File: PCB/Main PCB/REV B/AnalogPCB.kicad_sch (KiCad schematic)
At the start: 60 parts, among them J1 DF12NB_4.0_-20DP-0.5V_51_, J2 393570002, J3 393570002, J4 393570002, J5 393570002, J6 SJ3-35053D, Q1 2N7002, Q2 2N7002, Q3 2N7002, U1 ALDP105W, U2 ALDP105W, U3 ALDP105W

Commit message: Digital board revisions, changed to 0805 and started review of circuitry
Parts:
- removed C4: 10uF 16V X5R 0805, Capacitor_SMD:C_0805_2012Metric, symbol Device:C
- removed C?: 0.1uF 50V X7R 0805, Capacitor_SMD:C_0805_2012Metric, symbol Device:C
- removed PS2: IRM-05-5, Converter_ACDC:Converter_ACDC_MeanWell_IRM-05-xx_THT, symbol Converter_ACDC:IRM-05-5
- removed TP3: TP, TestPoint:TestPoint_Pad_D1.0mm, symbol Connector:TestPoint
- added C? (x3): 10uF 16V X5R 0805, Capacitor_SMD:C_0805_2012Metric, symbol Device:C
- added C?: 56uF 50V TH, Capacitor_THT:C_Radial_D10.0mm_H12.5mm_P5.00mm, symbol Device:C
- added L?: 5.6uH 2.9A, Customs Smoker:IND_IFSC-2020DE-01_VIS, symbol pspice:INDUCTOR
- added PS2: TSR-2-2433, Converter_DCDC:Converter_DCDC_TRACO_TSR-1_THT, symbol Regulator_Switching:TSR_1-2433
- added TP?: TP, TestPoint:TestPoint_Pad_D1.0mm, symbol Connector:TestPoint
- PS1: value IRM-10-3.3 -> IRM-10-5; Manufacturer Part Number IRM-10-3.3 -> IRM-10-5; Vendor Part Number 1866-3031-ND -> 1866-3032-ND
- gave numbers to parts that had none: 11
- renumbered D3 to D5, J2 to J1, J1 to J2, R4 to R7, R5 to R8, TP16 to TP1, TP20 to TP10, TP29 to TP11, TP18 to TP3, TP1 to TP4, TP17 to TP6, TP13 to TP7, TP15 to TP8, TP19 to TP9
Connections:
- net +3.3VA: now also C?.1, C?.2, L?.2, TP?.1; no longer C1.2, C2.1, PS1.4 (+Vo), TP4.1
- net +5V: now also C1.2, C2.1, PS1.4 (+Vo), TP4.1, PS2.1 (Vin)
- net GND: now also C?.1, C?.1, C?.2, C?.2, PS2.2 (GND)
- new net: C?.1, C?.2, L?.1, PS2.3 (Vout)
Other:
- note added: "ASSUME MEAT PROBE TIP 1-2 connection Measure resistance and room temp (1000ohms)"
- note added: "Power Delivery"
- note removed: "AC-DC MAIN"
- note removed: "ASSUME MEAT PROBE TIP 1-2 connection"
- note removed: "TODO Test this and fix"
- moved on the sheet: C1, C2, D5, D6, J1, PS1, R7, R8, TP1, TP3, TP4, TP7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

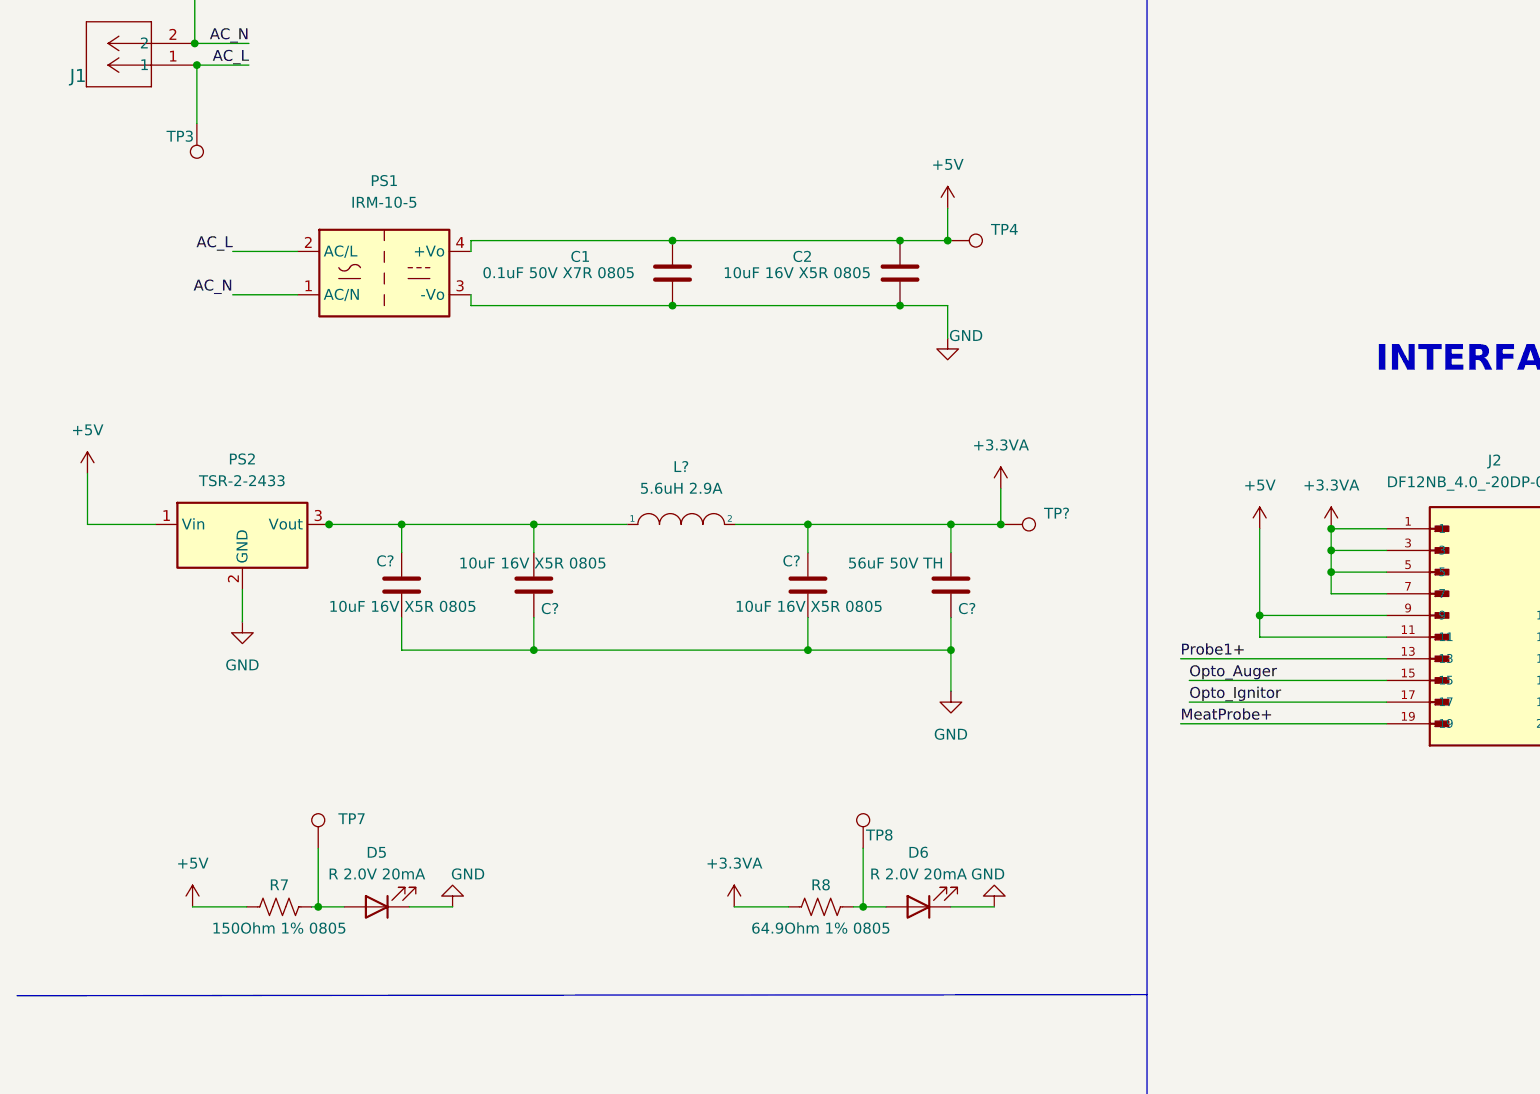
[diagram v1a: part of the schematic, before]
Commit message: begin change of power arch so mux occurs at 5.0v rather than 3.3v
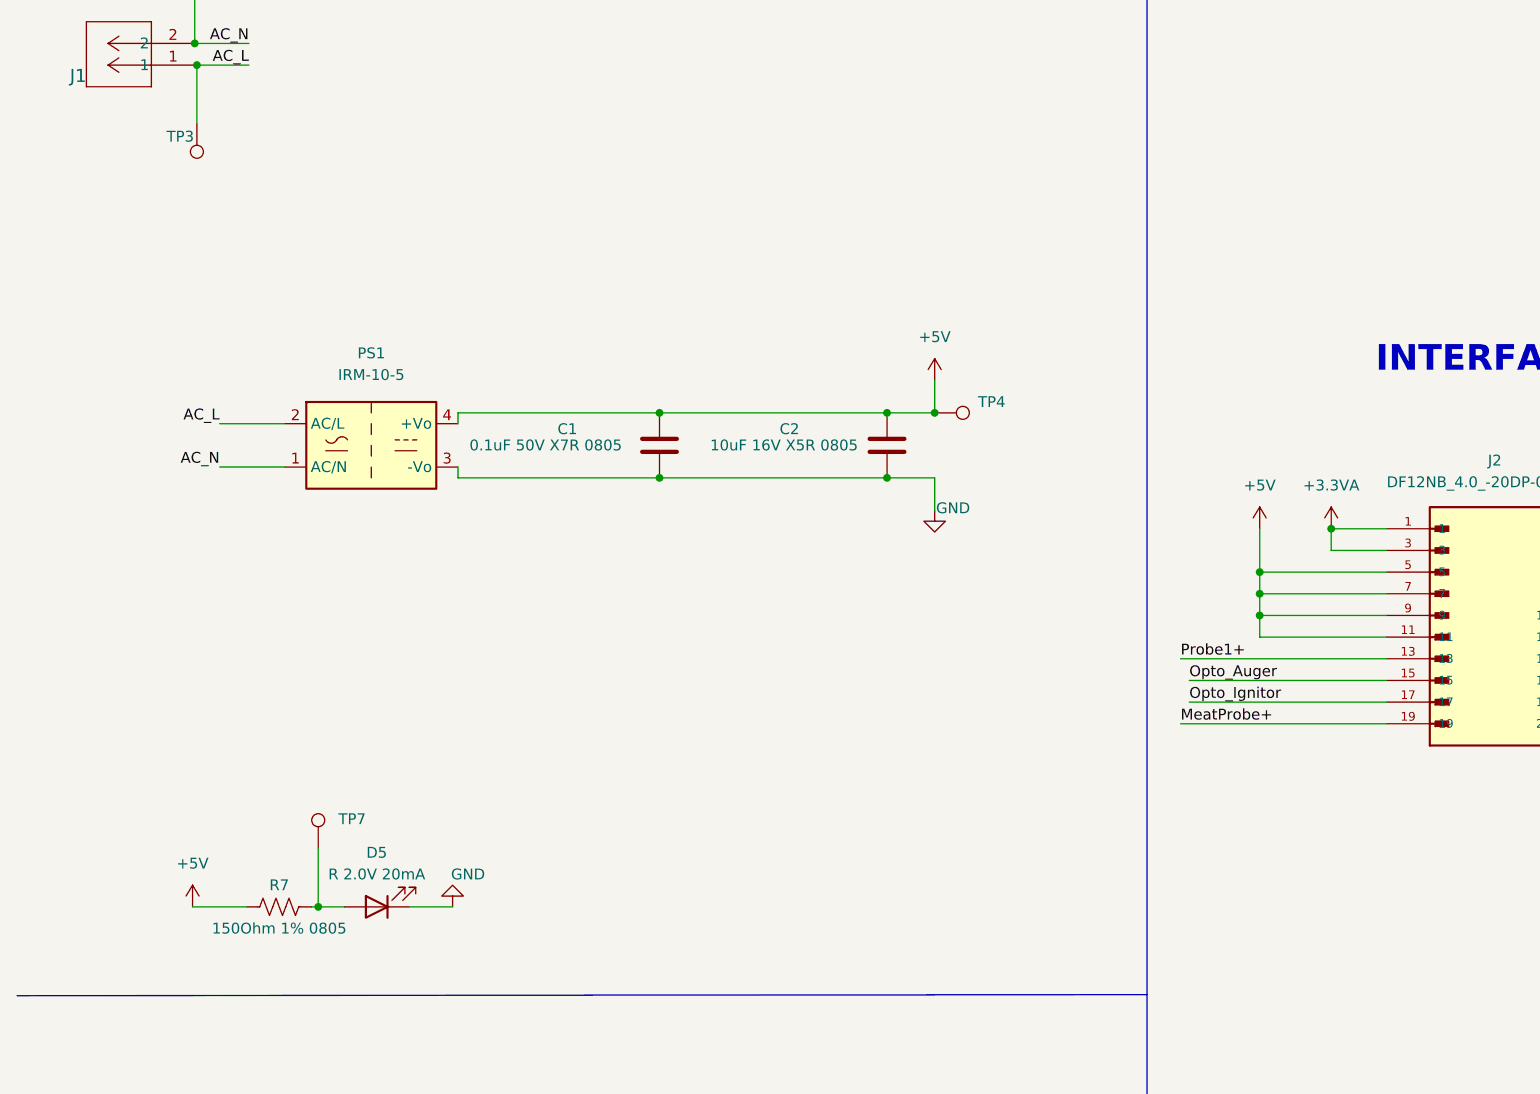
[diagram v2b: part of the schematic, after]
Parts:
- removed C? (x3): 10uF 16V X5R 0805, Capacitor_SMD:C_0805_2012Metric, symbol Device:C
- removed C?: 56uF 50V TH, Capacitor_THT:C_Radial_D10.0mm_H12.5mm_P5.00mm, symbol Device:C
- removed D6: R 2.0V 20mA, LED_SMD:LED_0805_2012Metric, symbol Device:LED
- removed L?: 5.6uH 2.9A, Customs Smoker:IND_IFSC-2020DE-01_VIS, symbol pspice:INDUCTOR
- removed PS2: TSR-2-2433, Converter_DCDC:Converter_DCDC_TRACO_TSR-1_THT, symbol Regulator_Switching:TSR_1-2433
- removed R8: 64.9Ohm 1% 0805, Resistor_SMD:R_0805_2012Metric, symbol Device:R_US
- removed TP8, TP?: TP, TestPoint:TestPoint_Pad_D1.0mm, symbol Connector:TestPoint
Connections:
- net +3.3VA: no longer J2.5, J2.7
- net +5V: now also J2.5, J2.7
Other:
- moved on the sheet: C1, C2, PS1, TP4
